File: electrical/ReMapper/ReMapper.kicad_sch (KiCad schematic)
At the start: 42 parts, among them J1 ESP_UART0, J2 I2C Display, J3 USB_IN, J4 USB_OUT, J5 Button GND Pad, J9 Button Socket, U1 SPX1117M3-L-3-3/TR, U2 W25Q128JVE, U3 ESP32-S3-WROOM-1-N8R8, U4 RP2040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

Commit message: started working on v5
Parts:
- removed J1: ESP_UART0, Connector_PinHeader_1.27mm:PinHeader_1x04_P1.27mm_Vertical_SMD_Pin1Right, symbol Connector:Conn_01x04_Pin
- removed J5: Button GND Pad, TestPoint:TestPoint_Pad_D2.0mm, symbol Connector:Conn_01x01_Pin
- removed J9: Button Socket, Connector_PinHeader_1.27mm:PinHeader_1x04_P1.27mm_Vertical_SMD_Pin1Left, symbol Connector:Conn_01x04_Pin
- removed JP1: RP2040 Prog, Jumper:SolderJumper-2_P1.3mm_Open_RoundedPad1.0x1.5mm, symbol Jumper:SolderJumper_2_Open
- added J5: PogoPIN, cedarhacks:pogo_pin_2.54mm, symbol Connector:Conn_01x06_Pin
- added S3: ESP_B1, generated_lscs:SW-SMD_4P-L4.5-W4.5-P3.00-LS6.8, symbol push_button_SKRPABE010:SKRPABE010
- added S4: ESP_B2, generated_lscs:SW-SMD_4P-L4.5-W4.5-P3.00-LS6.8, symbol push_button_SKRPABE010:SKRPABE010
- added S5: ESP_B3, generated_lscs:SW-SMD_4P-L4.5-W4.5-P3.00-LS6.8, symbol push_button_SKRPABE010:SKRPABE010
- added S6: ESP_B4_prog, generated_lscs:SW-SMD_4P-L4.5-W4.5-P3.00-LS6.8, symbol push_button_SKRPABE010:SKRPABE010
- J2: footprint Connector_PinHeader_1.27mm:PinHeader_1x04_P1.27mm_Vertical -> Connector_PinHeader_2.54mm:PinHeader_1x04_P2.54mm_Vertical
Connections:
- net 3.3V: now also J5.1 (Pin_1)
- net ESP_BUTTON_1: now also S3.1, S3.2
- net ESP_BUTTON_2: now also S4.1, S4.2
- net ESP_BUTTON_3: now also S5.1, S5.2
- net ESP_RXDO: now also J5.3 (Pin_3)
- net ESP_TXDO: now also J5.2 (Pin_2)
- net GND: now also J5.4 (Pin_4), J5.6 (Pin_6), S3.3, S3.4, S4.3, S4.4, S5.3, S5.4, S6.3, S6.4
- net RP2040_PROG: now reaches R5.1
- net RP2040_PROG: now also J5.5 (Pin_5)
- new net: S6.1, S6.2

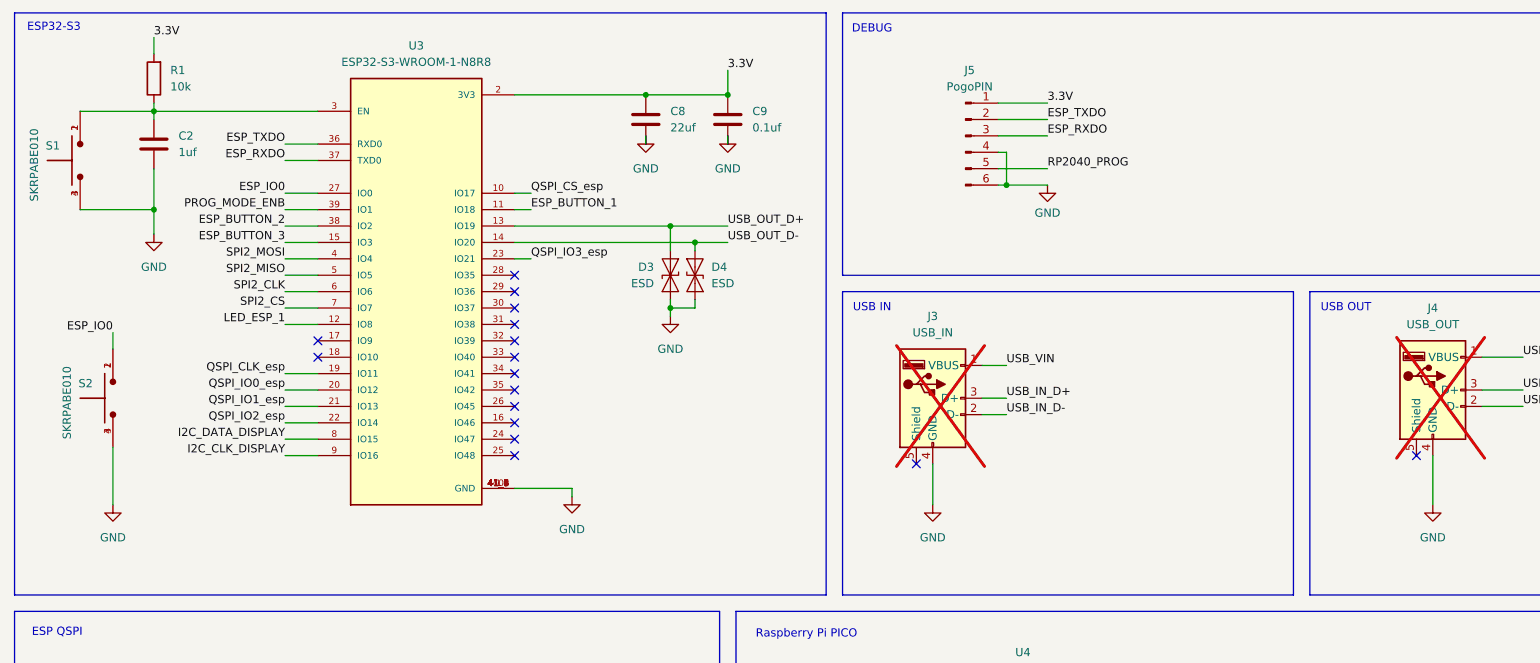
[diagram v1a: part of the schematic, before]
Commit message: dip switch, more layout fixes
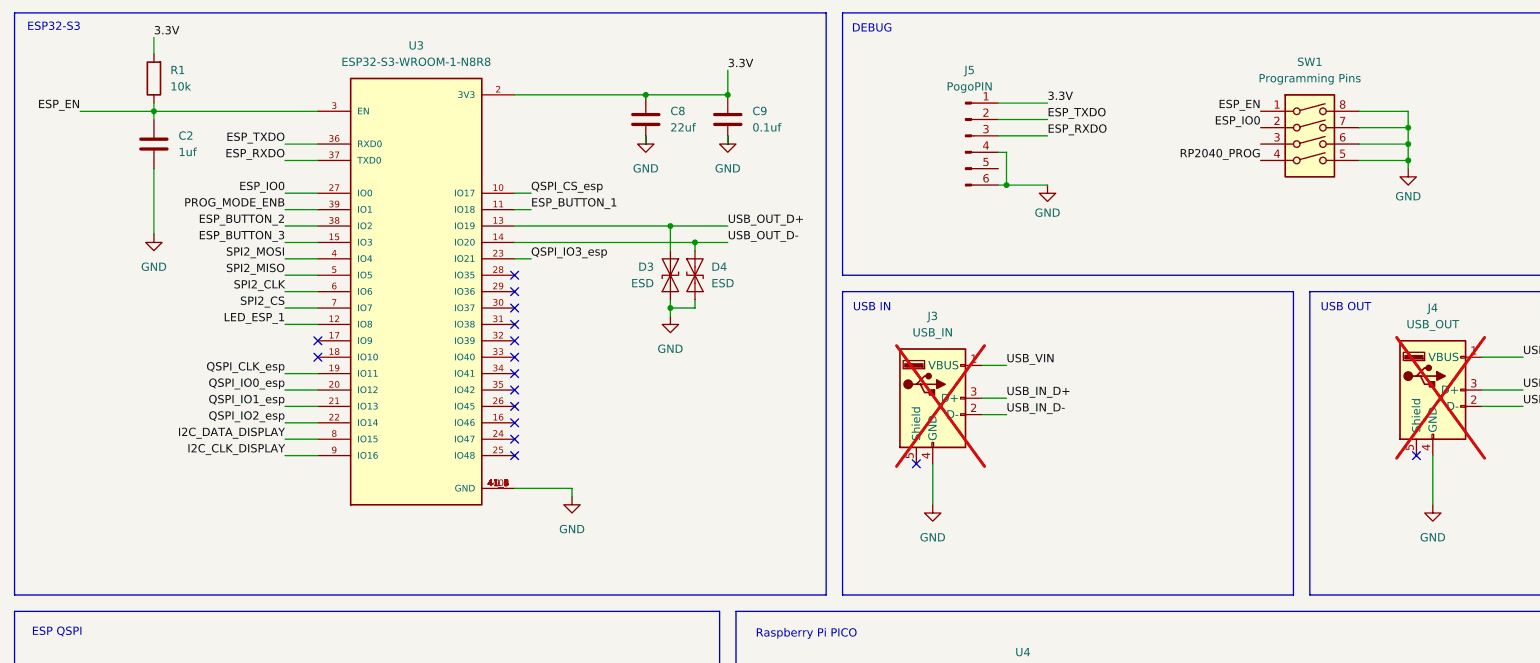
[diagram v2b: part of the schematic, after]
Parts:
- removed S1, S2: SKRPABE010, footprints:push_button_SKRPABE010, symbol push_button_SKRPABE010:SKRPABE010
- added SW1: Programming Pins, footprints:SW_DIP_219-4, symbol Switch:SW_DIP_x04
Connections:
- net ESP_IO0: now also SW1.2
- net GND: now also SW1.5, SW1.6, SW1.7, SW1.8
- net RP2040_PROG: now also SW1.4; no longer J5.5 (Pin_5)
- net ESP_EN: now reaches C2.1, R1.1, U3.3 (EN)
- net ESP_EN: now also SW1.1

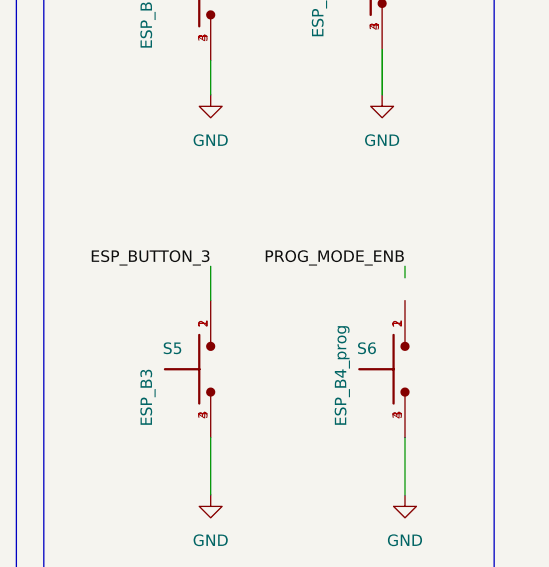
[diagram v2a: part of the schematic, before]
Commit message: passing DRC
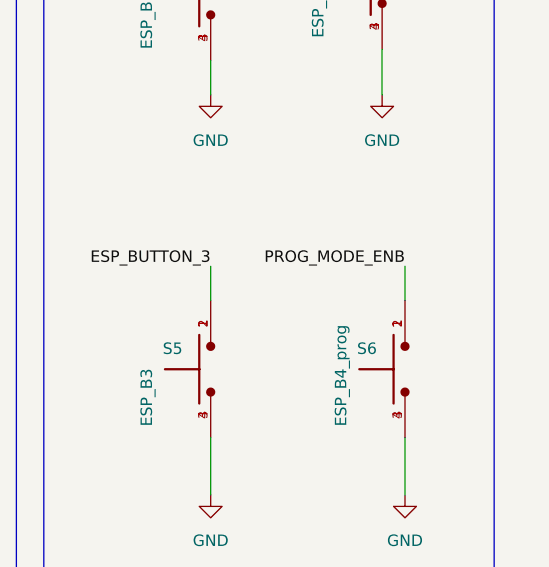
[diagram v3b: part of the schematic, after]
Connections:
- net PROG_MODE_ENB: now also S6.1, S6.2
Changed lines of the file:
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@@
-	(wire
-		(pts
-			(xy 392.43 163.83) (xy 392.43 165.1)
-		)
-		(stroke
-			(width 0)
-			(type default)
-		)
-	)
 	(wire
 		(pts
@@
 		)
 		(stroke
+			(width 0)
+			(type default)
+		)
+	)
+	(wire
+		(pts
+			(xy 392.43 163.83) (xy 392.43 167.64)
+		)
+		(stroke
